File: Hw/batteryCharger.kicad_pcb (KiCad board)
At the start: 2 copper layers, 12.2 x 17.4 mm, 12 parts, among them J1 Vcc, J2 GND, J3 BAT, J4 GND, U1 MCP73831-2-OT

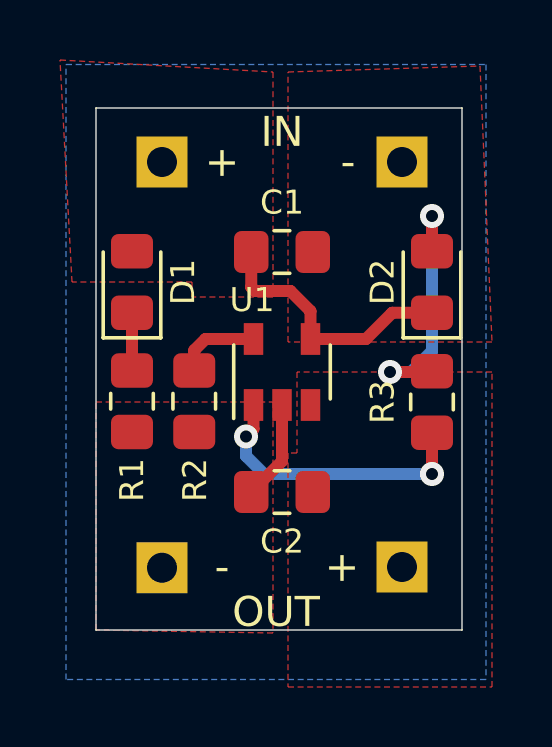
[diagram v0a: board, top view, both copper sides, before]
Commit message: Udate jumper for faster charge add logos
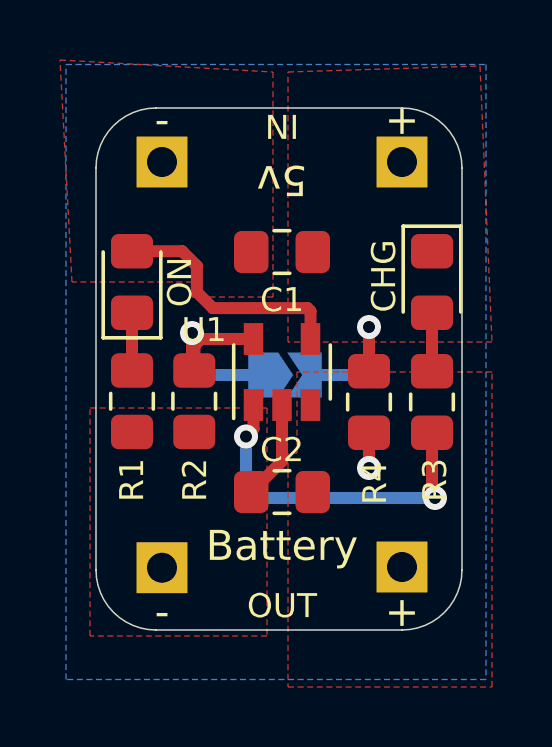
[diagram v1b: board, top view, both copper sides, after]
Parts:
- added G***: LOGO, Aesthetics:electronic_cats_logo_4x3, B.Cu at (135.0, 94.1)
- added JP1: JP1, Jumper:SolderJumper-2_P1.3mm_Open_TrianglePad1.0x1.5mm, B.Cu at (135.1, 98.1)
- added R4: 2.5K, Resistor_SMD:R_0805_2012Metric_Pad1.15x1.40mm_HandSolder, F.Cu at (137.9, 99.0)
- C1: value C -> 10uF
- moved J1 8.00 mm to (139.0, 91.0)
- moved J2 8.00 mm to (131.0, 91.0)
- turned C1 to 180 degrees
- turned D2 to 270 degrees
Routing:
- net Net-(JP1-Pad1): track 2.81 -> 11.2 mm, vias 0 -> 1
- net Net-(D2-Pad2): track 8.78 -> 1.95 mm, vias 2 -> 0
- net Net-(JP1-Pad2): track 0.00 -> 4.98 mm, vias 0 -> 1
- net Net-(R3-Pad1): track 9.63 -> 11.4 mm
- net GND: track 3.32 -> 4.50 mm, vias 0 -> 1
- net VCC: track 8.82 -> 8.22 mm
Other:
- outline, holes or cut-outs redrawn
- board text added: "5v"
- board text added: "Battery"
- board text added: "CHG"
- board text added: "ON"

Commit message: Update_kicad_6
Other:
- net class Default removed
